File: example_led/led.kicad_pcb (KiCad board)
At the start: 2 copper layers, 4 parts, among them P1 IN, P2 OUT

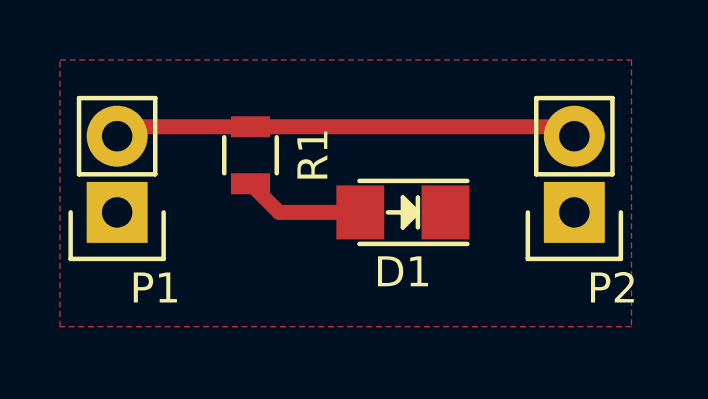
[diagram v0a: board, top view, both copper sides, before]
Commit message: Recursive example
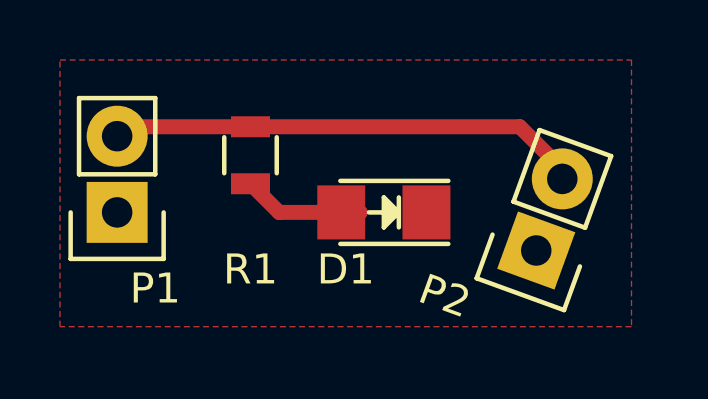
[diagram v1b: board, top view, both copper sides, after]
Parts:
- moved P2 1.80 mm to (144.8, 132.1), turned to 160 degrees
- moved D1 0.64 mm to (139.7, 130.8)
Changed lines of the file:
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@@
     (links 5)
     (no_connects 0)
-    (area 128.905 125.73 147.955001 134.620001)
+    (area 128.578096 125.73 148.496191 134.620001)
     (thickness 1.6)
     (drawings 0)
@@
   )
   (module Pin_Headers:Pin_Header_Straight_1x02 (layer F.Cu)
-    (at 146.05 130.81 180)
+    (at 144.78 132.08 160)
     (descr "Through hole pin header")
     (tags "pin header")
-    (fp_text reference P2 (at -1.27 -2.54 180) (layer F.SilkS)
-      (effects (font (size 1 1) (thickness 0.15)))
-    )
-    (fp_text value OUT (at 1.27 -2.54 180) (layer F.Fab)
+    (fp_text reference P2 (at 2.342944 -2.474569 160) (layer F.SilkS)
+      (effects (font (size 1 1) (thickness 0.15)))
+    )
+    (fp_text value OUT (at 1.507486 4.892557 160) (layer F.Fab)
       (effects (font (size 1 1) (thickness 0.15)))
     )
@@
     (fp_line (start -1.27 1.27) (end -1.27 3.81) (layer F.SilkS) (width 0.15))
     (fp_line (start -1.27 3.81) (end 1.27 3.81) (layer F.SilkS) (width 0.15))
-    (pad 1 thru_hole rect (at 0 0 180) (size 2.032 2.032) (drill 1.016) (layers *.Cu *.Mask F.SilkS)
+    (pad 1 thru_hole rect (at 0 0 160) (size 2.032 2.032) (drill 1.016) (layers *.Cu *.Mask F.SilkS)
       (net 3 Earth))
-    (pad 2 thru_hole oval (at 0 2.54 180) (size 2.032 2.032) (drill 1.016) (layers *.Cu *.Mask F.SilkS)
+    (pad 2 thru_hole oval (at 0 2.54 160) (size 2.032 2.032) (drill 1.016) (layers *.Cu *.Mask F.SilkS)
       (net 2 "Net-(P1-Pad2)"))
     (model Pin_Headers.3dshapes/Pin_Header_Straight_1x02.wrl
@@
     (tags "resistor 0805")
     (attr smd)
-    (fp_text reference R1 (at 0 -2.1 270) (layer F.SilkS)
+    (fp_text reference R1 (at 3.81 0 360) (layer F.SilkS)
       (effects (font (size 1 1) (thickness 0.15)))
     )
@@
   )
   (module LEDs:LED_1206 (layer F.Cu)
-    (at 140.335 130.81 180)
+    (at 139.7 130.81 180)
     (descr "LED 1206 smd package")
     (tags "LED1206 SMD")
     (attr smd)
-    (fp_text reference D1 (at 0 -2 180) (layer F.SilkS)
+    (fp_text reference D1 (at 1.27 -1.905 180) (layer F.SilkS)
       (effects (font (size 1 1) (thickness 0.15)))
     )
@@
   (segment (start 138.91514 130.81) (end 136.21 130.81) (width 0.5) (layer F.Cu) (net 1))
   (segment (start 136.21 130.81) (end 135.255 129.855) (width 0.5) (layer F.Cu) (net 1))
-  (segment (start 135.255 127.955) (end 145.735 127.955) (width 0.5) (layer F.Cu) (net 2) (status 20))
-  (segment (start 145.735 127.955) (end 146.05 128.27) (width 0.5) (layer F.Cu) (net 2) (status 30))
+  (segment (start 135.255 127.955) (end 144.232478 127.955) (width 0.5) (layer F.Cu) (net 2))
+  (segment (start 144.232478 127.955) (end 145.856066 129.578588) (width 0.5) (layer F.Cu) (net 2))
   (segment (start 135.255 127.955) (end 131.125 127.955) (width 0.5) (layer F.Cu) (net 2) (status 20))
   (segment (start 131.125 127.955) (end 130.81 128.27) (width 0.5) (layer F.Cu) (net 2) (status 30))
